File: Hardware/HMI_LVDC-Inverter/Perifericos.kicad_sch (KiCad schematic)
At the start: 55 parts, among them J8 Conn_01x04_Pin, K1 G5LE-1, Q1 BC847, Q2 2N7002, Q3 2N7002, SW1 SW_MEC_5E, SW2 SW_MEC_5E, SW3 SW_MEC_5E, SW4 SW_MEC_5E, SW5 SW_MEC_5E, SW6 SW_MEC_5E, SW7 SW_MEC_5E, SW8 SW_MEC_5E, U1 4N25, U10 4N25, U24 PC817, U5 4N25, U6 4N25, U7 4N25, U8 4N25, U9 4N25

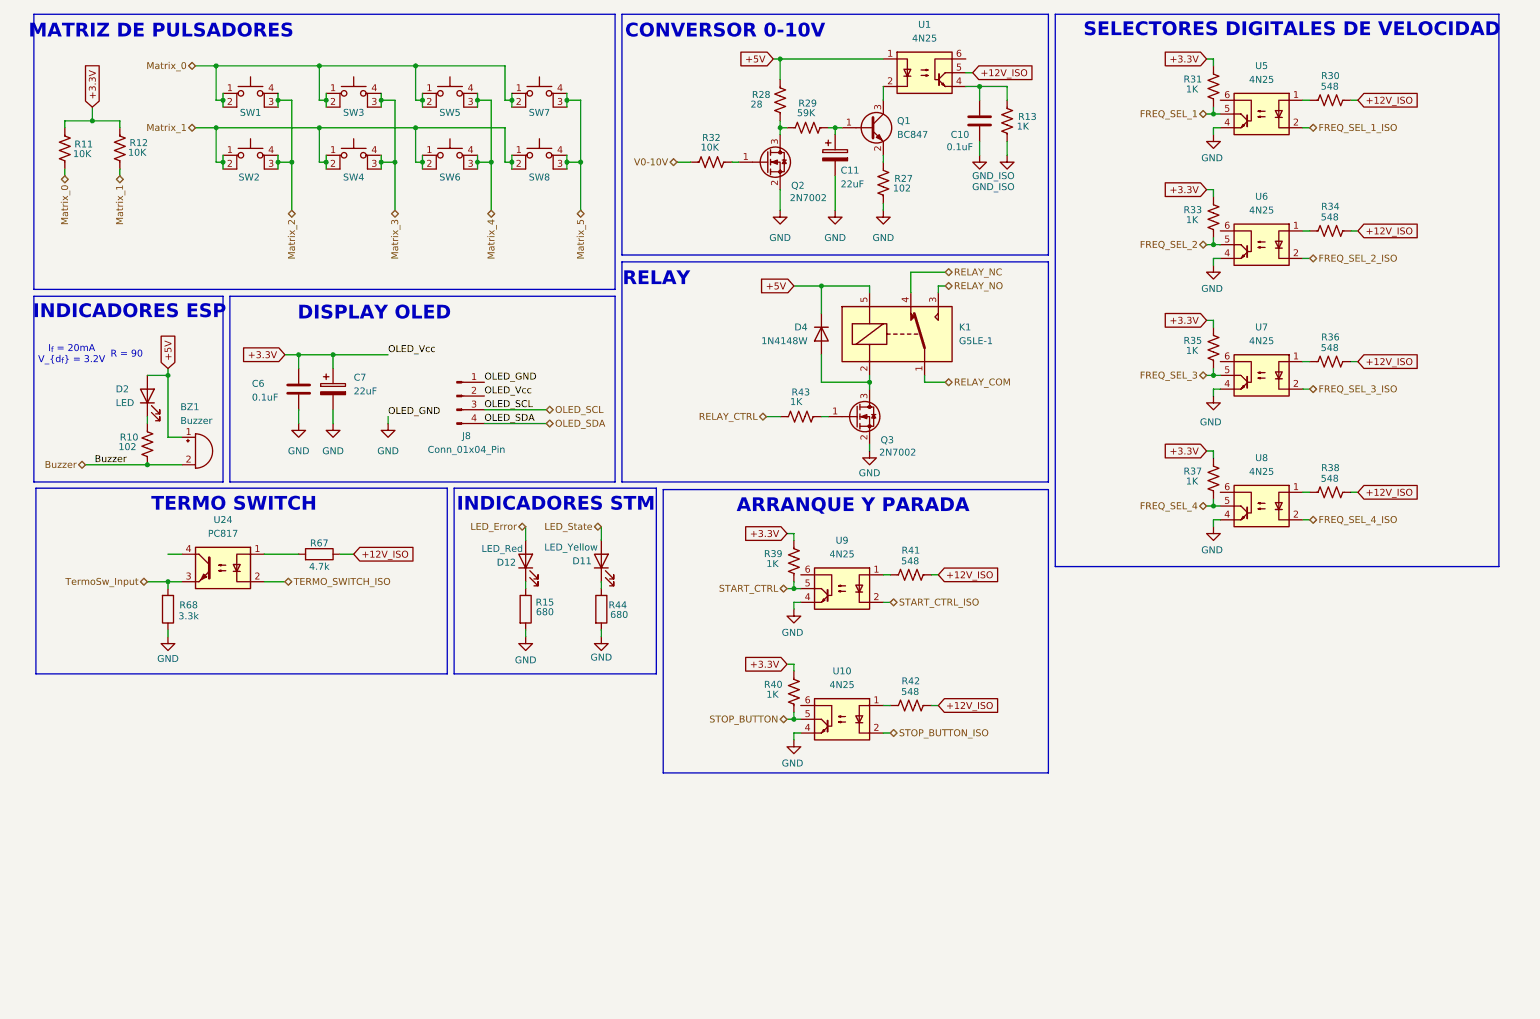
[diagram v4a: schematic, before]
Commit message: Terminado todo el conexionado eléctrico esquemático
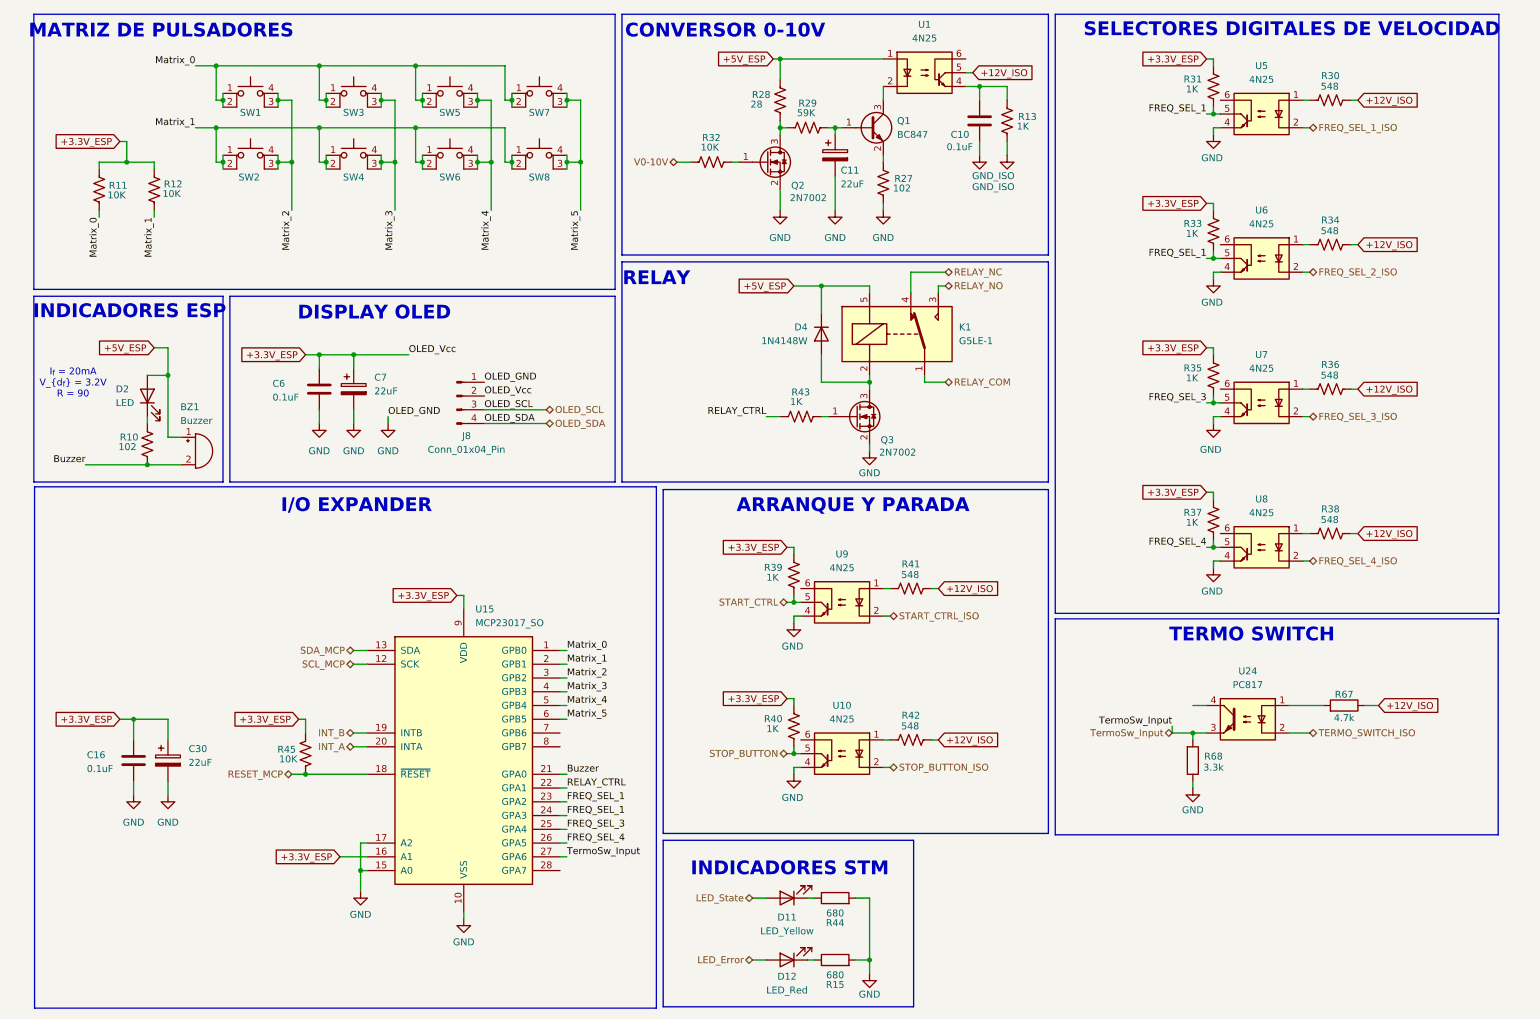
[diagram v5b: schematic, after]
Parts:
- added C16: 0.1uF, Capacitor_SMD:C_0603_1608Metric, symbol Device:C
- added C30: 22uF, Capacitor_SMD:C_1206_3216Metric, symbol Device:C_Polarized
- added R45: 10K, symbol Device:R_US
- added U15: MCP23017_SO, Package_SO:SOIC-28W_7.5x17.9mm_P1.27mm, symbol Interface_Expansion:MCP23017_SO
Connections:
- net FREQ_SEL_2 is gone; now on net FREQ_SEL_1: R33.1, U6.5
- net Buzzer: now also U15.21 (GPA0)
- net FREQ_SEL_1: now also U15.23 (GPA2), U15.24 (GPA3)
- net FREQ_SEL_3: now also U15.25 (GPA4)
- net FREQ_SEL_4: now also U15.26 (GPA5)
- net GND: now also C16.2, C30.2, U15.10 (VSS), U15.15 (A0), U15.17 (A2)
- net Matrix_0: now also U15.1 (GPB0)
- net Matrix_1: now also U15.2 (GPB1)
- net Matrix_2: now also U15.3 (GPB2)
- net Matrix_3: now also U15.4 (GPB3)
- net Matrix_4: now also U15.5 (GPB4)
- net Matrix_5: now also U15.6 (GPB5)
- net RELAY_CTRL: now also U15.22 (GPA1)
- net TermoSw_Input: now also U15.27 (GPA6)
- net +3.3V renamed +3.3V_ESP
- net +3.3V_ESP: now also C16.1, C30.1, R45.1, U15.16 (A1), U15.9 (VDD)
- net +5V renamed +5V_ESP
- new net INT_A: U15.20 (INTA)
- new net INT_B: U15.19 (INTB)
- new net RESET_MCP: R45.2, U15.18 (~{RESET})
- new net SCL_MCP: U15.12 (SCK)
- new net SDA_MCP: U15.13 (SDA)
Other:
- note added: "I/O EXPANDER"
- company: (none) -> Andrenacci - Carra
- title: (none) -> Variador de frecuencia LVDC
- moved on the sheet: C6, C7, D11, D12, R11, R12, R15, R33, R34, R35, R36, R37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

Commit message: Agregado de los componentes con links de compra en KiCAD a excepción de los conectores
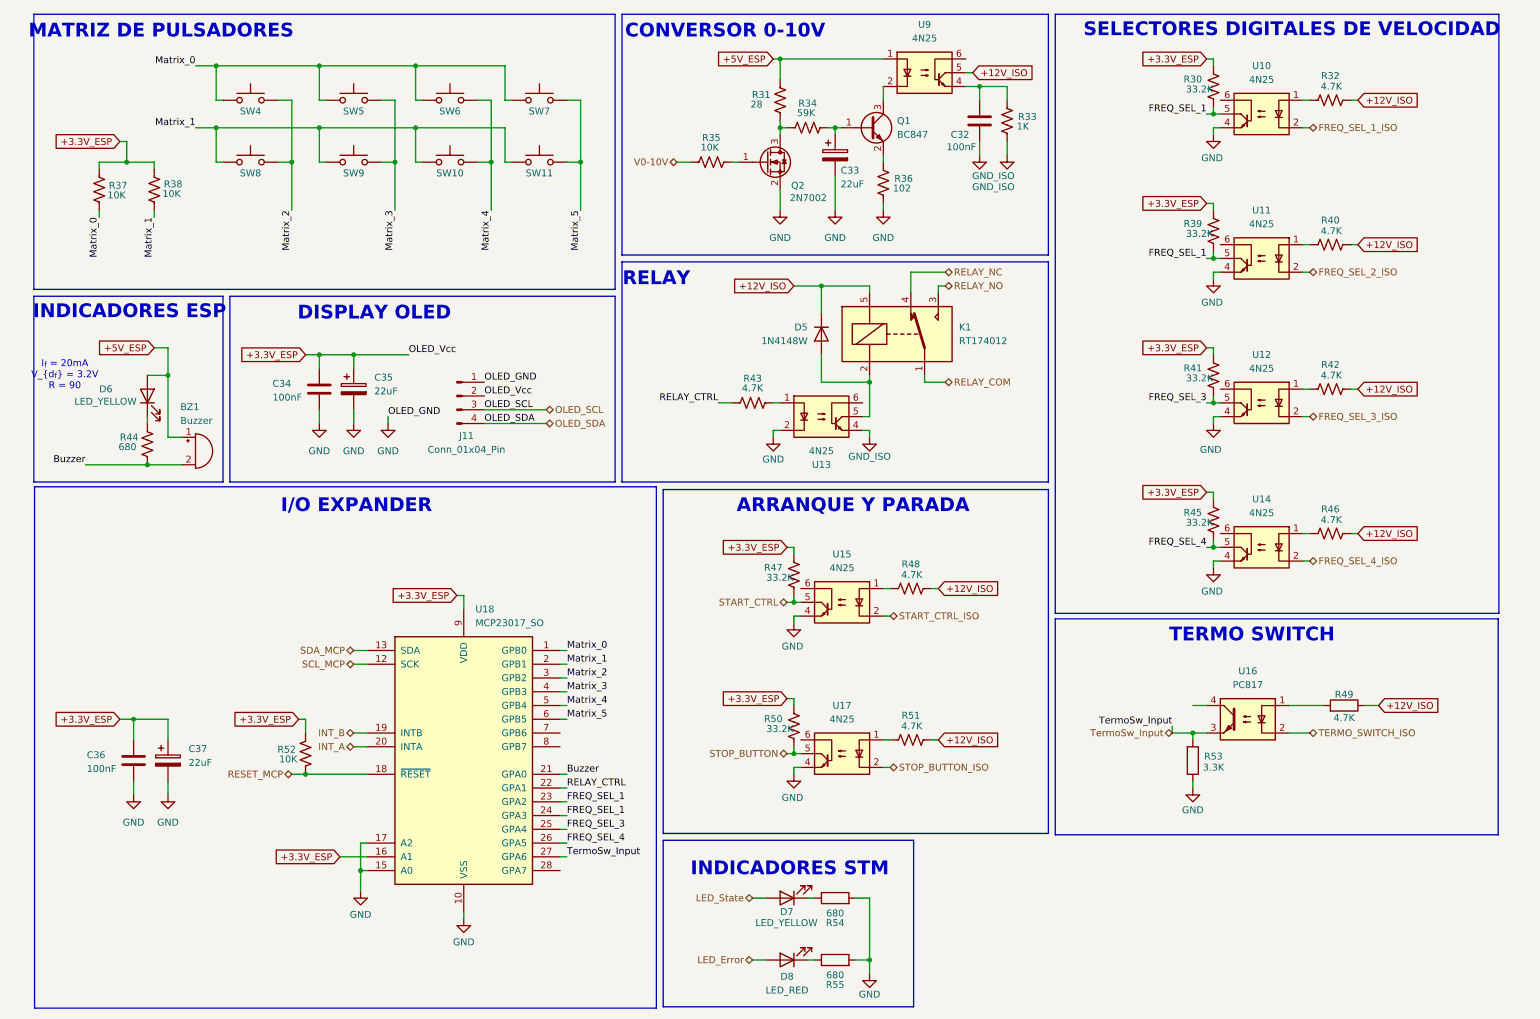
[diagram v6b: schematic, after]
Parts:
- removed D11: LED_Yellow, LED_SMD:LED_0603_1608Metric_Pad1.05x0.95mm_HandSolder, symbol Device:LED
- removed Q3: 2N7002, Package_TO_SOT_SMD:SOT-23, symbol Transistor_FET:2N7002
- removed SW1, SW2, SW3, SW4, SW5, SW6, SW7, SW8: SW_MEC_5E, Button_Switch_SMD:SW_MEC_5GSH9, symbol Switch:SW_MEC_5E
- added D7: LED_YELLOW, LED_SMD:LED_0603_1608Metric_Pad1.05x0.95mm_HandSolder, symbol Device:LED
- added SW10, SW11, SW4, SW5, SW6, SW7, SW8, SW9: SW_MEC_5G, symbol Switch:SW_MEC_5G
- added U13: 4N25, Package_DIP:DIP-6_W7.62mm_SMDSocket_SmallPads, symbol Isolator:4N25
- BZ1: footprint (none) -> Buzzer_Beeper:Buzzer_12x9.5RM7.6; Compra (none) -> https://www.lcsc.com/product-detail/C96222.html; Footprint checked (none) -> Yes; Manufacturer (none) -> Huaneng; Symbol checked (none) -> Yes; currier https://ar.mouser.com/ProductDetail/539-ASI09N27MFD05TRQ -> (none)
- C32: renamed from C10; value 0.1uF -> 100nF; footprint Capacitor_SMD:C_0603_1608Metric -> Capacitor_SMD:C_0603_1608Metric_Pad1.08x0.95mm_HandSolder; Compra (none) -> https://www.lcsc.com/product-detail/C14663.html; Footprint checked (none) -> Yes; Manufacturer (none) -> Yagueo; Price 0.1 -> 0.24; Symbol checked (none) -> Yes; currier https://ar.mouser.com/ProductDetail/YAGEO/CC0603KRX7R7BB104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 -> (none)
- C33: renamed from C11; footprint Capacitor_SMD:C_1206_3216Metric -> Capacitor_SMD:CP_Elec_5x5.4; Compra (none) -> https://www.lcsc.com/product-detail/C72502.html; Footprint checked (none) -> Yes; Manufacturer (none) -> Roquang; Price 0.6 -> 0.41; Symbol checked (none) -> Yes; currier https://ar.mouser.com/ProductDetail/TAIYO-YUDEN/EMK316BB722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 -> (none)
- C34: renamed from C6; value 0.1uF -> 100nF; footprint Capacitor_SMD:C_0603_1608Metric -> Capacitor_SMD:C_0603_1608Metric_Pad1.08x0.95mm_HandSolder; Compra (none) -> https://www.lcsc.com/product-detail/C14663.html; Footprint checked (none) -> Yes; Manufacturer (none) -> Yagueo; Price 0.1 -> 0.24; Symbol checked (none) -> Yes; currier https://ar.mouser.com/ProductDetail/YAGEO/CC0603KRX7R7BB104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 -> (none)
- C35: renamed from C7; footprint Capacitor_SMD:C_1206_3216Metric -> Capacitor_SMD:CP_Elec_5x5.4; Compra (none) -> https://www.lcsc.com/product-detail/C72502.html; Footprint checked (none) -> Yes; Manufacturer (none) -> Roquang; Price 0.6 -> 0.41; Symbol checked (none) -> Yes; currier https://ar.mouser.com/ProductDetail/TAIYO-YUDEN/EMK316BB722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 -> (none)
- C36: renamed from C16; value 0.1uF -> 100nF; footprint Capacitor_SMD:C_0603_1608Metric -> Capacitor_SMD:C_0603_1608Metric_Pad1.08x0.95mm_HandSolder; Compra (none) -> https://www.lcsc.com/product-detail/C14663.html; Footprint checked (none) -> Yes; Manufacturer (none) -> Yagueo; Price 0.1 -> 0.24; Symbol checked (none) -> Yes; currier https://ar.mouser.com/ProductDetail/YAGEO/CC0603KRX7R7BB104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 -> (none)
- C37: renamed from C30; footprint Capacitor_SMD:C_1206_3216Metric -> Capacitor_SMD:CP_Elec_5x5.4; Compra (none) -> https://www.lcsc.com/product-detail/C72502.html; Footprint checked (none) -> Yes; Manufacturer (none) -> Roquang; Price 0.6 -> 0.41; Symbol checked (none) -> Yes; currier https://ar.mouser.com/ProductDetail/TAIYO-YUDEN/EMK316BB722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 -> (none)
- D5: renamed from D4; Compra (none) -> https://www.lcsc.com/product-detail/C241939.html?s_z=n_1N41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; Footprint checked (none) -> Yes; Manufacturer (none) -> VISHAY; Price (none) -> 0.0338; Symbol checked (none) -> Yes
- D6: renamed from D2; value LED -> LED_YELLOW; footprint LED_SMD:LED_0805_2012Metric_Pad1.15x1.40mm_HandSolder -> LED_SMD:LED_0603_1608Metric_Pad1.05x0.95mm_HandSolder; Compra (none) -> https://www.lcsc.com/product-detail/C965802.html; Footprint checked (none) -> Yes; Manufacturer (none) -> XINGLIGHT; Price 0.63 -> 0.0059; Symbol checked (none) -> Yes; currier https://ar.mouser.com/ProductDetail/Dialight/599-0181-007F?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 -> (none)
- D8: renamed from D12; value LED_Red -> LED_RED; Compra (none) -> https://www.lcsc.com/product-detail/C965799.html; Footprint checked (none) -> Yes; Manufacturer (none) -> XINGLIGHT; Price (none) -> 0.0032; Symbol checked (none) -> Yes
- K1: value G5LE-1 -> RT174012; footprint Relay_THT:Relay_SPDT_Omron_G2RL-1 -> Relay_THT:Relay_SPDT_Panasonic_JW1_FormC; Compra (none) -> https://www.lcsc.com/product-detail/C6460993.html; Manufacturer (none) -> TE Connectivity; Price 1.33 -> 6.0068; Symbol checked (none) -> Yes; currier https://ar.mouser.com/ProductDetail/Omron-Electronics/G5LE-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 -> (none)
- Q1: footprint Package_TO_SOT_THT:TO-39-3 -> Package_TO_SOT_SMD:SOT-523; Compra (none) -> https://www.lcsc.com/product-detail/C526465.html?s_z=n_BC84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; Footprint checked (none) -> Yes; Manufacturer (none) -> DIODES; Price 0.2 -> 0.0379; Symbol checked (none) -> Yes; currier https://ar.mouser.com/ProductDetail/Rectron/BC847?qs=7pEAo9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 -> (none)
- Q2: Compra (none) -> https://www.lcsc.com/product-detail/C81445.html?s_z=n_2N7002; Footprint checked (none) -> Yes; Manufacturer (none) -> VISHAY; Symbol checked (none) -> Yes; currier https://ar.mouser.com/ProductDetail/Diodes-Incorporated/BC8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 -> (none)
- R30: renamed from R31; value 1K -> 33.2K; footprint (none) -> Resistor_SMD:R_0603_1608Metric_Pad0.98x0.95mm_HandSolder; Compra (none) -> https://www.lcsc.com/product-detail/C706161.html; Footprint checked (none) -> Yes; Manufacturer (none) -> YAGEO; Price (none) -> 0.0095; Symbol checked (none) -> Yes
- R31: renamed from R28; footprint (none) -> Resistor_SMD:R_1210_3225Metric_Pad1.30x2.65mm_HandSolder; Compra (none) -> https://www.lcsc.com/product-detail/C7079269.html; Footprint checked (none) -> Yes; Manufacturer (none) -> KOA; Symbol checked (none) -> Yes
- R32: renamed from R30; value 548 -> 4.7K; footprint (none) -> Resistor_SMD:R_0603_1608Metric_Pad0.98x0.95mm_HandSolder; Compra (none) -> https://www.lcsc.com/product-detail/C2078630.html; Footprint checked (none) -> Yes; Manufacturer (none) -> VISHAY; Price (none) -> 0.0220; Symbol checked (none) -> Yes
- R33: renamed from R13; footprint (none) -> Resistor_SMD:R_0603_1608Metric_Pad0.98x0.95mm_HandSolder; Compra (none) -> https://www.lcsc.com/product-detail/C2653986.html; Footprint checked (none) -> Yes; Manufacturer (none) -> ROHM; Price (none) -> 0.0123; Symbol checked (none) -> Yes
- R34: renamed from R29; footprint (none) -> Resistor_SMD:R_0603_1608Metric_Pad0.98x0.95mm_HandSolder; Compra (none) -> https://www.lcsc.com/product-detail/C203697.html; Footprint checked (none) -> Yes; Manufacturer (none) -> BOURNS; Price (none) -> 0.0087; Symbol checked (none) -> Yes
- R35: renamed from R32; footprint (none) -> Resistor_SMD:R_0603_1608Metric_Pad0.98x0.95mm_HandSolder; Compra (none) -> https://www.lcsc.com/product-detail/C491211.html; Footprint checked (none) -> Yes; Manufacturer (none) -> PANASONIC; Price (none) -> 0.0321; Symbol checked (none) -> Yes
- R36: renamed from R27; footprint (none) -> Resistor_SMD:R_0603_1608Metric_Pad0.98x0.95mm_HandSolder; Compra (none) -> https://www.lcsc.com/product-detail/C4191024.html; Footprint checked (none) -> Yes; Manufacturer (none) -> VISHAY; Symbol checked (none) -> Yes
- R37: renamed from R11; footprint (none) -> Resistor_SMD:R_0603_1608Metric_Pad0.98x0.95mm_HandSolder; Compra (none) -> https://www.lcsc.com/product-detail/C491211.html; Footprint checked (none) -> Yes; Manufacturer (none) -> PANASONIC; Price (none) -> 0.0321; Symbol checked (none) -> Yes
- R38: renamed from R12; footprint (none) -> Resistor_SMD:R_0603_1608Metric_Pad0.98x0.95mm_HandSolder; Compra (none) -> https://www.lcsc.com/product-detail/C491211.html; Footprint checked (none) -> Yes; Manufacturer (none) -> PANASONIC; Price (none) -> 0.0321; Symbol checked (none) -> Yes
- R39: renamed from R33; value 1K -> 33.2K; footprint (none) -> Resistor_SMD:R_0603_1608Metric_Pad0.98x0.95mm_HandSolder; Compra (none) -> https://www.lcsc.com/product-detail/C706161.html; Footprint checked (none) -> Yes; Manufacturer (none) -> YAGEO; Price (none) -> 0.0095; Symbol checked (none) -> Yes
- R40: renamed from R34; value 548 -> 4.7K; footprint (none) -> Resistor_SMD:R_0603_1608Metric_Pad0.98x0.95mm_HandSolder; Compra (none) -> https://www.lcsc.com/product-detail/C2078630.html; Footprint checked (none) -> Yes; Manufacturer (none) -> VISHAY; Price (none) -> 0.0220; Symbol checked (none) -> Yes
- R41: renamed from R35; value 1K -> 33.2K; footprint (none) -> Resistor_SMD:R_0603_1608Metric_Pad0.98x0.95mm_HandSolder; Compra (none) -> https://www.lcsc.com/product-detail/C706161.html; Footprint checked (none) -> Yes; Manufacturer (none) -> YAGEO; Price (none) -> 0.0095; Symbol checked (none) -> Yes
- R42: renamed from R36; value 548 -> 4.7K; footprint (none) -> Resistor_SMD:R_0603_1608Metric_Pad0.98x0.95mm_HandSolder; Compra (none) -> https://www.lcsc.com/product-detail/C2078630.html; Footprint checked (none) -> Yes; Manufacturer (none) -> VISHAY; Price (none) -> 0.0220; Symbol checked (none) -> Yes
- R43: value 1K -> 4.7K; footprint (none) -> Resistor_SMD:R_0603_1608Metric_Pad0.98x0.95mm_HandSolder; Compra (none) -> https://www.lcsc.com/product-detail/C2078630.html; Footprint checked (none) -> Yes; Manufacturer (none) -> VISHAY; Price (none) -> 0.0220; Symbol checked (none) -> Yes
- R44: renamed from R10; value 102 -> 680; footprint (none) -> Resistor_SMD:R_0603_1608Metric_Pad0.98x0.95mm_HandSolder; Compra (none) -> https://www.lcsc.com/product-detail/C20109434.html; Footprint checked (none) -> Yes; Manufacturer (none) -> ROHM; Price (none) -> 0.0186; Symbol checked (none) -> Yes
- R45: renamed from R37; value 1K -> 33.2K; footprint (none) -> Resistor_SMD:R_0603_1608Metric_Pad0.98x0.95mm_HandSolder; Compra (none) -> https://www.lcsc.com/product-detail/C706161.html; Footprint checked (none) -> Yes; Manufacturer (none) -> YAGEO; Price (none) -> 0.0095; Symbol checked (none) -> Yes
- R46: renamed from R38; value 548 -> 4.7K; footprint (none) -> Resistor_SMD:R_0603_1608Metric_Pad0.98x0.95mm_HandSolder; Compra (none) -> https://www.lcsc.com/product-detail/C2078630.html; Footprint checked (none) -> Yes; Manufacturer (none) -> VISHAY; Price (none) -> 0.0220; Symbol checked (none) -> Yes
- R47: renamed from R39; value 1K -> 33.2K; footprint (none) -> Resistor_SMD:R_0603_1608Metric_Pad0.98x0.95mm_HandSolder; Compra (none) -> https://www.lcsc.com/product-detail/C706161.html; Footprint checked (none) -> Yes; Manufacturer (none) -> YAGEO; Price (none) -> 0.0095; Symbol checked (none) -> Yes
- R48: renamed from R41; value 548 -> 4.7K; footprint (none) -> Resistor_SMD:R_0603_1608Metric_Pad0.98x0.95mm_HandSolder; Compra (none) -> https://www.lcsc.com/product-detail/C2078630.html; Footprint checked (none) -> Yes; Manufacturer (none) -> VISHAY; Price (none) -> 0.0220; Symbol checked (none) -> Yes
- R49: renamed from R67; value 4.7k -> 4.7K; Compra (none) -> https://www.lcsc.com/product-detail/C2078630.html; Footprint checked (none) -> Yes; Manufacturer (none) -> VISHAY; Price (none) -> 0.0220; Symbol checked (none) -> Yes
- R50: renamed from R40; value 1K -> 33.2K; footprint (none) -> Resistor_SMD:R_0603_1608Metric_Pad0.98x0.95mm_HandSolder; Compra (none) -> https://www.lcsc.com/product-detail/C706161.html; Footprint checked (none) -> Yes; Manufacturer (none) -> YAGEO; Price (none) -> 0.0095; Symbol checked (none) -> Yes
- R51: renamed from R42; value 548 -> 4.7K; footprint (none) -> Resistor_SMD:R_0603_1608Metric_Pad0.98x0.95mm_HandSolder; Compra (none) -> https://www.lcsc.com/product-detail/C2078630.html; Footprint checked (none) -> Yes; Manufacturer (none) -> VISHAY; Price (none) -> 0.0220; Symbol checked (none) -> Yes
- R52: renamed from R45; footprint (none) -> Resistor_SMD:R_0603_1608Metric_Pad0.98x0.95mm_HandSolder; Compra (none) -> https://www.lcsc.com/product-detail/C491211.html; Footprint checked (none) -> Yes; Manufacturer (none) -> PANASONIC; Price (none) -> 0.0321; Symbol checked (none) -> Yes
- R53: renamed from R68; value 3.3k -> 3.3K; Compra (none) -> https://www.lcsc.com/product-detail/C4098385.html; Footprint checked (none) -> Yes; Manufacturer (none) -> VISHAY; Price (none) -> 0.0301; Symbol checked (none) -> Yes
- R54: renamed from R44; Compra (none) -> https://www.lcsc.com/product-detail/C20109434.html; Footprint checked (none) -> Yes; Manufacturer (none) -> ROHM; Price (none) -> 0.0186; Symbol checked (none) -> Yes
- R55: renamed from R15; Compra (none) -> https://www.lcsc.com/product-detail/C20109434.html; Footprint checked (none) -> Yes; Manufacturer (none) -> ROHM; Price (none) -> 0.0186; Symbol checked (none) -> Yes
- U10: renamed from U5; Compra (none) -> https://www.lcsc.com/product-detail/C898941.html?s_z=n_4N25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; Manufacturer (none) -> onsemi; Price (none) -> 0.9182
- U11: renamed from U6; Compra (none) -> https://www.lcsc.com/product-detail/C898941.html?s_z=n_4N25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; Manufacturer (none) -> onsemi; Price (none) -> 0.9182
- U12: renamed from U7; Compra (none) -> https://www.lcsc.com/product-detail/C898941.html?s_z=n_4N25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; Manufacturer (none) -> onsemi; Price (none) -> 0.9182
- U14: renamed from U8; Compra (none) -> https://www.lcsc.com/product-detail/C898941.html?s_z=n_4N25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; Manufacturer (none) -> onsemi; Price (none) -> 0.9182
- U15: renamed from U9; Compra (none) -> https://www.lcsc.com/product-detail/C898941.html?s_z=n_4N25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; Manufacturer (none) -> onsemi; Price (none) -> 0.9182
- U16: renamed from U24; Compra (none) -> https://www.lcsc.com/product-detail/C3008368.html; Manufacturer (none) -> UMW; Price (none) -> 0.0347
- U17: renamed from U10; Compra (none) -> https://www.lcsc.com/product-detail/C898941.html?s_z=n_4N25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; Manufacturer (none) -> onsemi; Price (none) -> 0.9182
- U18: renamed from U15; Compra (none) -> https://www.lcsc.com/product-detail/C629440.html?s_z=n_MCP2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; Footprint checked (none) -> Yes; Manufacturer (none) -> Microchip; Price (none) -> 1.9379; Symbol checked (none) -> Yes
- U9: renamed from U1; Compra (none) -> https://www.lcsc.com/product-detail/C898941.html?s_z=n_4N25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; Manufacturer (none) -> onsemi; Price (none) -> 0.9182
- renumbered J8 to J11
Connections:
- net +12V_ISO: now also D5.1 (K), K1.5
- net +5V_ESP: no longer D5.1 (K), K1.5
- net GND: now also U13.2
- net GND_ISO: now also U13.4
- net LED_State: now also D7.2 (A)
- net Matrix_0: now also SW4.1 (A), SW4.2 (A), SW5.1 (A), SW5.2 (A), SW6.1 (A), SW6.2 (A), SW7.1 (A), SW7.2 (A)
- net Matrix_1: now also SW10.1 (A), SW10.2 (A), SW11.1 (A), SW11.2 (A), SW8.1 (A), SW8.2 (A), SW9.1 (A), SW9.2 (A)
- net Matrix_2: now also SW4.3 (B), SW4.4 (B), SW8.3 (B), SW8.4 (B)
- net Matrix_3: now also SW5.3 (B), SW5.4 (B), SW9.3 (B), SW9.4 (B)
- net Matrix_4: now also SW10.3 (B), SW10.4 (B), SW6.3 (B), SW6.4 (B)
- net Matrix_5: now also SW11.3 (B), SW11.4 (B), SW7.3 (B), SW7.4 (B)
- net at D5.2 (A), K1.2: now also U13.5
- net at R43.2: now also U13.1
- net at R54.1: now also D7.1 (K)
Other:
- moved on the sheet: R43

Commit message: Avances en el PCB, arreglos en el esquema y agregado de borneras de gabinete
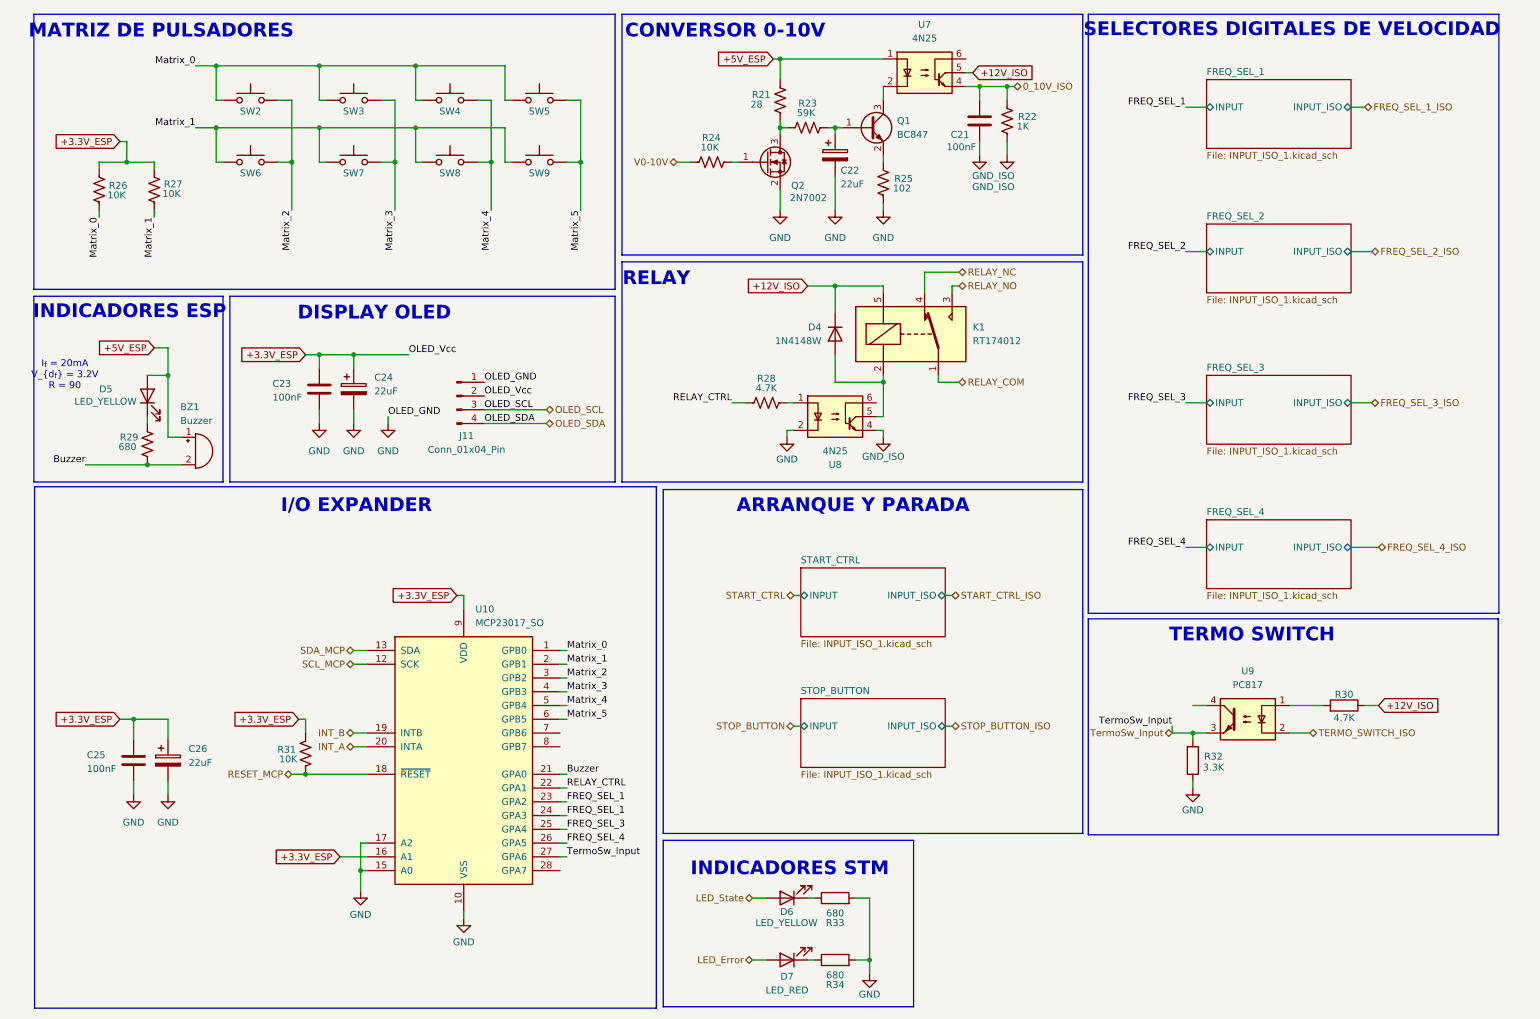
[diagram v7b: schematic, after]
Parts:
- removed R30, R39, R41, R45, R47, R50: 33.2K, Resistor_SMD:R_0603_1608Metric_Pad0.98x0.95mm_HandSolder, symbol Device:R_US
- removed R32, R40, R42, R46, R48, R51: 4.7K, Resistor_SMD:R_0603_1608Metric_Pad0.98x0.95mm_HandSolder, symbol Device:R_US
- removed U10, U11, U12, U14, U15, U17: 4N25, Package_DIP:DIP-6_W7.62mm_SMDSocket_SmallPads, symbol Isolator:4N25
- K1: footprint Relay_THT:Relay_SPDT_Panasonic_JW1_FormC -> Footprints:RT174012
- renumbered C32 to C21, C33 to C22, C34 to C23, C35 to C24, C36 to C25, C37 to C26, D5 to D4, D6 to D5, D7 to D6, D8 to D7, R31 to R21, R33 to R22, R34 to R23, R35 to R24, R36 to R25, R37 to R26, R38 to R27, R43 to R28, R44 to R29, R49 to R30, R52 to R31, R53 to R32, R54 to R33, R55 to R34, SW4 to SW2, SW5 to SW3, SW6 to SW4, SW7 to SW5, SW8 to SW6, SW9 to SW7, SW10 to SW8, SW11 to SW9, U18 to U10, U9 to U7, U13 to U8, U16 to U9
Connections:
- net 0_10V_ISO: now reaches C21.1, R22.2, U7.4
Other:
- added sheet FREQ_SEL_1 (INPUT_ISO_1.kicad_sch)
- added sheet FREQ_SEL_2 (INPUT_ISO_1.kicad_sch)
- added sheet FREQ_SEL_3 (INPUT_ISO_1.kicad_sch)
- added sheet FREQ_SEL_4 (INPUT_ISO_1.kicad_sch)
- added sheet START_CTRL (INPUT_ISO_1.kicad_sch)
- added sheet STOP_BUTTON (INPUT_ISO_1.kicad_sch)
- moved on the sheet: D4, K1, R28, U8

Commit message: Falta resolver los pulsadores
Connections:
- net FREQ_SEL_1: no longer U10.24 (GPA3)
- net FREQ_SEL_2: now also U10.24 (GPA3)
- net 3V3_STM: now reaches U9.4
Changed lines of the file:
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@@
+	(wire
+		(pts
+			(xy 226.06 140.97) (xy 229.87 140.97)
+		)
+		(stroke
+			(width 0)
+			(type default)
+		)
+	)
 	(wire
 		(pts
@@
 		(pts
 			(xy 110.49 156.21) (xy 111.76 156.21)
-		)
-		(stroke
-			(width 0)
-			(type default)
-		)
-	)
-	(wire
-		(pts
-			(xy 229.87 140.97) (xy 227.33 140.97)
 		)
 		(stroke
@@
 		)
 	)
-	(label "FREQ_SEL_1"
+	(label "FREQ_SEL_2"
 		(at 111.76 161.29 0)
 		(effects
@@
 			)
 			(justify right bottom)
+		)
+	)
+	(global_label "3V3_STM"
+		(shape input)
+		(at 226.06 140.97 180)
+		(fields_autoplaced yes)
+		(effects
+			(font
+				(size 1.27 1.27)
+			)
+			(justify right)
+		)
+		(property "Intersheetrefs" "${INTERSHEET_REFS}"
+			(at 213.5196 140.97 0)
+			(effects
+				(font
+					(size 1.27 1.27)
+				)
+				(justify right)
+				(hide yes)
+			)
 		)
 	)
@@
 			(effects
 				(font
-					(size 1.27 1.27)
-					(italic yes)
-				)
-			)
-		)
-	)
-	(netclass_flag ""
-		(length 2.54)
-		(shape round)
-		(at 227.33 140.97 0)
-		(effects
-			(font
-				(size 1.27 1.27)
-			)
-			(justify left bottom)
-		)
-		(property "Netclass" "3.3V_STM"
-			(at 231.902 136.398 0)
-			(effects
-				(font
-					(size 1.27 1.27)
-				)
-				(justify right)
-			)
-		)
-		(property "Component Class" ""
-			(at 508 66.04 0)
-			(effects
-				(font
